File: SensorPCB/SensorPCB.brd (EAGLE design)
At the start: 36 x 66 mm, 31 parts, among them T1 33u

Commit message: 3v almost ready
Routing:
- net +3V3: track 22.2 -> 173.0 mm, vias 1 -> 7
- net I2C1_SDA_SENSOR: track 48.6 -> 71.7 mm, vias 0 -> 2
- net SW_WLAN: track 31.7 -> 32.9 mm
- net PB0: track 69.9 -> 69.0 mm
- net USART2_RX_SENSOR: track 122.6 -> 123.3 mm
- net SWCLK: track 10.4 -> 9.71 mm

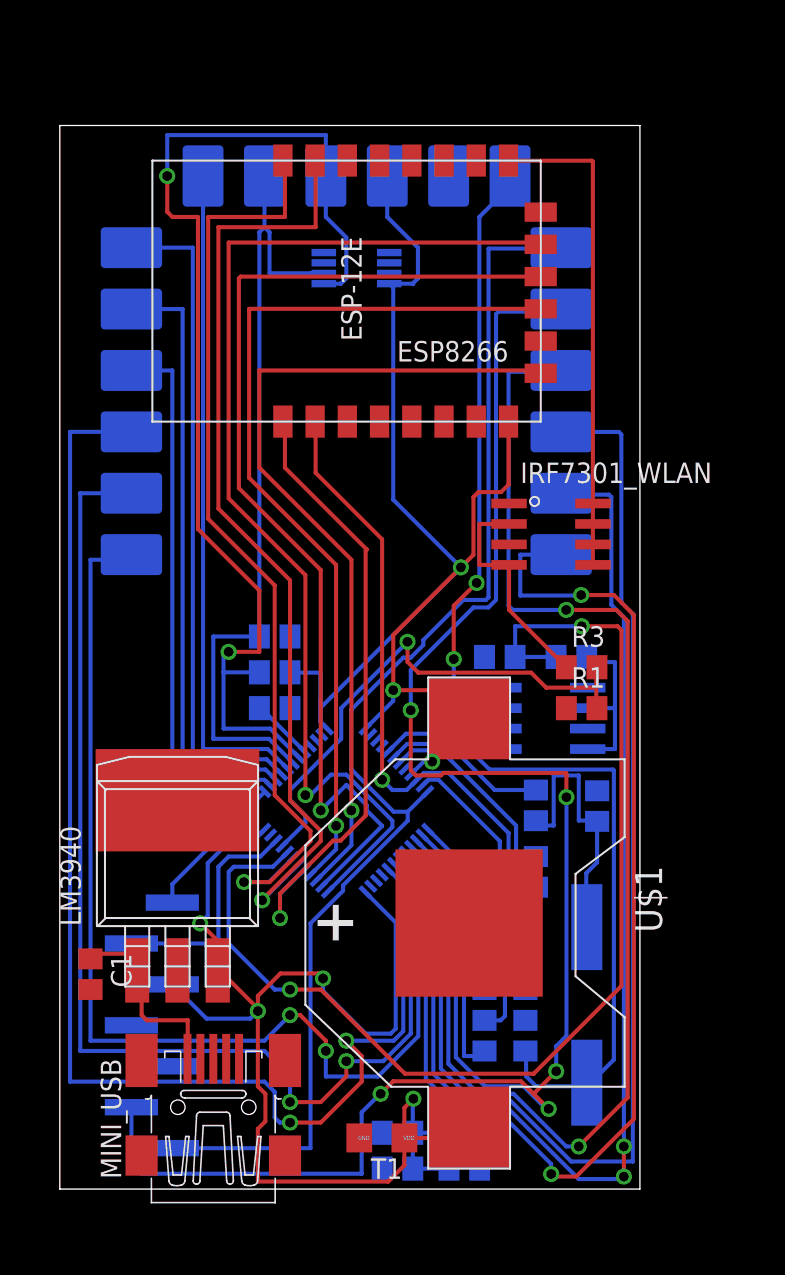
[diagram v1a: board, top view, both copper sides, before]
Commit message: routed all 3v wires
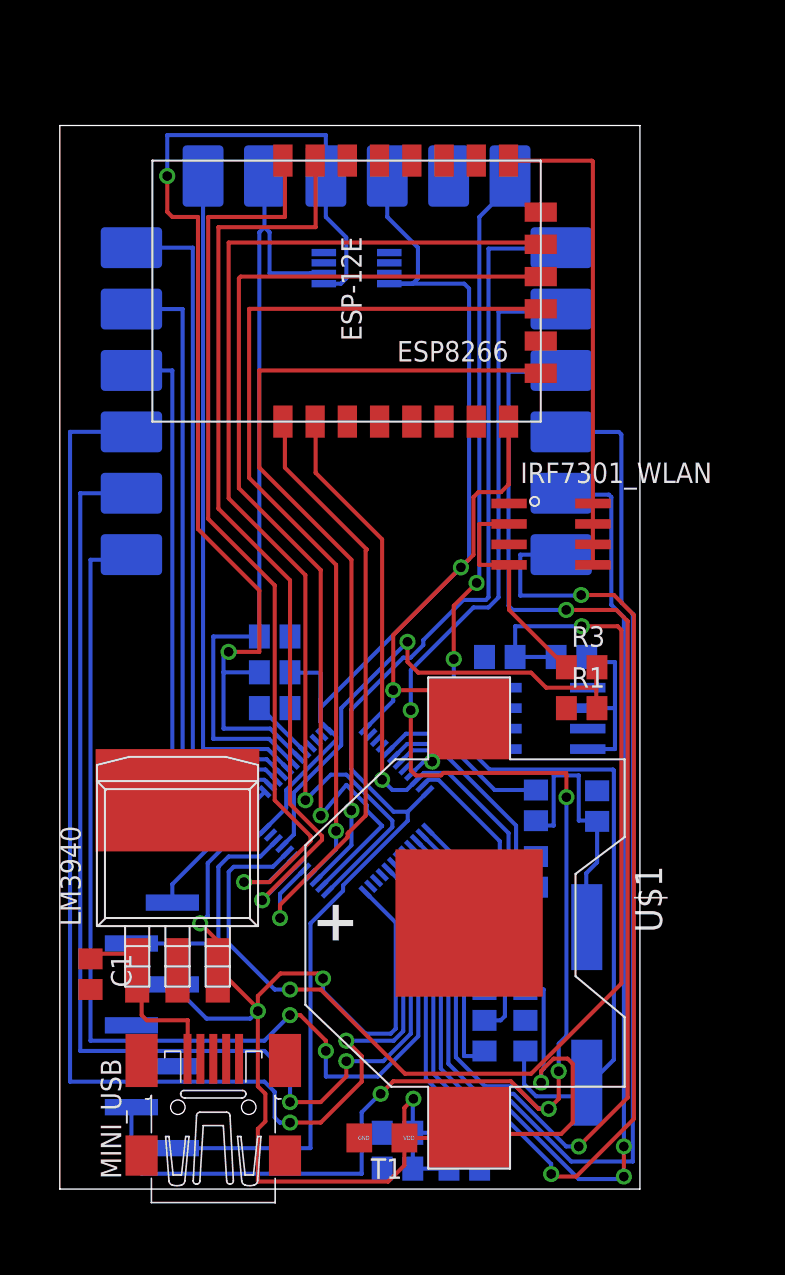
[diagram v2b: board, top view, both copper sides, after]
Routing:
- net +3V3: track 173.0 -> 204.4 mm, vias 7 -> 8
- net OSC_IN: track 41.6 -> 42.8 mm
- net SW_WLAN: track 32.9 -> 32.1 mm
- net SPI2_SCK_WLAN: track 64.9 -> 65.5 mm
- net USART2_RX_SENSOR: track 123.3 -> 123.8 mm

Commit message: start new board version
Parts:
- removed MINI_USB: MINI-USB-SCHIELD-32005-201, con-cypressindustries:32005-201
- added R4: 10k, rcl:R0805
- added U$2: 5V_POWER_SUPPLY, 5V_POWER_SUPPLY:5V_POWER_SUPPLY
- moved T1 30.8 mm to (6.99, 31.1)
- moved R1 27.8 mm to (5.08, 24.8), flipped to the bottom, turned to 180 degrees
- moved R6 24.7 mm to (5.08, 22.2)
- moved C6 21.3 mm to (34.6, 2.54), flipped to the top, turned to 0 degrees
- moved R10 20.9 mm to (34.0, 28.9)
- moved R3 20.6 mm to (12.1, 35.6)
- moved ESP8266 19.1 mm to (10.8, 45.7), turned to 0 degrees
- moved R11 19.1 mm to (34.6, 5.40), flipped to the top, turned to 0 degrees
- moved IRF7301_WLAN 18.5 mm to (12.1, 39.4)
- moved R7 18.2 mm to (34.0, 26.0), turned to 0 degrees
- moved C1 17.8 mm to (2.22, 31.1), turned to 180 degrees
- moved QUARZ-HC49 14.1 mm to (34.3, 25.4), flipped to the top, turned to 90 degrees
- moved C8 12.9 mm to (15.2, 9.53), turned to 0 degrees
- moved C10 12.9 mm to (34.0, 31.8), turned to 0 degrees
- moved C3 12.8 mm to (15.2, 12.7)
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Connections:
- removed net CH_PD_WLAN: ESP8266.3
- removed net D+: MINI_USB.3
- removed net D-: MINI_USB.2
- removed net ID: MINI_USB.4
- new net ADC: R7.2, R8.1, STM32L051C8T6.10
- new net CHPD: ESP8266.3, R4.1
- net +3V3: now also R4.2
- net +5V: now also U$2.MINUS; no longer MINI_USB.1
- net ADC_WLAN: no longer R7.2, R8.1, STM32L051C8T6.10
- net GND: now also U$2.PLUS; no longer MINI_USB.5
- net SPI2_MISO_WLAN: no longer STM32L051C8T6.27
- net SPI2_MOSI_WLAN: no longer STM32L051C8T6.28
- net SPI2_NSS_WLAN: no longer STM32L051C8T6.25
- net SPI2_SCK_WLAN: no longer STM32L051C8T6.26
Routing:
- net +3V3: track 204.4 -> 0.00 mm, vias 8 -> 0
- net USART2_RX_SENSOR: track 123.8 -> 0.00 mm, vias 5 -> 0
- net PA4: track 84.7 -> 0.00 mm, vias 2 -> 0
- net PB2: track 82.4 -> 0.00 mm, vias 2 -> 0
- net USART2_TX_SENSOR: track 80.1 -> 0.00 mm
- net PA5: track 78.3 -> 0.00 mm
- net PA7: track 75.8 -> 0.00 mm, vias 2 -> 0
- net PA6: track 75.1 -> 0.00 mm, vias 2 -> 0
- net PB1: track 73.9 -> 0.00 mm, vias 2 -> 0
- net SW_SENSOR: track 71.7 -> 0.00 mm, vias 2 -> 0
- net I2C1_SDA_SENSOR: track 71.7 -> 0.00 mm, vias 2 -> 0
- net SPI2_NSS_WLAN: track 69.3 -> 0.00 mm, vias 1 -> 0
- net PB0: track 69.0 -> 0.00 mm, vias 2 -> 0
- net SPI2_SCK_WLAN: track 65.5 -> 0.00 mm, vias 1 -> 0
- net USART1_TX_WLAN: track 59.4 -> 0.00 mm, vias 1 -> 0
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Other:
- board size 36 x 66 mm -> 37 x 70 mm

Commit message: some changes
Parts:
- moved R10 31.5 mm to (2.54, 26.4)
- moved PHD 20.7 mm to (24.4, 3.81), turned to 0 degrees
- moved C3 19.8 mm to (34.9, 10.5), turned to 270 degrees
- moved R6 10.2 mm to (7.94, 12.4)
- moved R1 9.94 mm to (7.94, 15.2)
- moved C5 8.90 mm to (30.5, 12.4), turned to 0 degrees
- moved C7 8.89 mm to (30.5, 9.53), turned to 0 degrees
- moved C8 7.30 mm to (7.94, 9.53), turned to 180 degrees
- moved C9 6.43 mm to (30.5, 15.2), turned to 180 degrees
- moved R9 5.97 mm to (2.54, 23.8)
- moved R8 3.19 mm to (34.3, 26.4), turned to 180 degrees
- moved R12 3.17 mm to (2.54, 28.9)
- moved C10 2.88 mm to (34.3, 28.9), turned to 180 degrees
- moved R7 2.25 mm to (34.3, 23.8)
- moved MCP9808 1.93 mm to (19.1, 55.6)
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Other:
- board size 37 x 70 mm -> 37 x 65 mm

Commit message: routing
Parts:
- moved C1 24.9 mm to (3.17, 6.19), turned to 0 degrees
- moved C4 23.5 mm to (34.1, 37.8), turned to 270 degrees
- moved U$2 23.3 mm to (5.40, 2.38), turned to 180 degrees
- moved MCP9808 20.3 mm to (3.97, 69.2)
- moved C6 15.3 mm to (35.6, 17.8), turned to 90 degrees
- moved IRF7301_SENSOR 12.7 mm to (12.1, 39.4)
- moved IRF7301_WLAN 12.7 mm to (24.8, 39.4)
- moved R2 12.7 mm to (12.1, 35.6)
- moved R3 12.7 mm to (24.8, 35.6)
- moved R11 12.5 mm to (32.7, 17.8), turned to 90 degrees
- moved LM3940 11.2 mm to (6.67, 24.1), turned to 0 degrees
- moved STM32L051C8T6 3.82 mm to (18.5, 23.0)
- moved T1 2.66 mm to (9.53, 31.9)
- moved U$1 2.54 mm to (21.0, 9.68)
- moved QUARZ-HC49 2.23 mm to (34.1, 27.6)
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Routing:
- net USART2_RX_SENSOR: track 0.00 -> 62.0 mm, vias 0 -> 2
- net USART2_TX_SENSOR: track 0.00 -> 60.0 mm, vias 0 -> 2
- net I2C1_SDA_SENSOR: track 0.00 -> 43.3 mm
- net PB2: track 0.00 -> 42.0 mm
- net I2C1_SCL_SENSOR: track 0.00 -> 40.5 mm
- net SPI1_MOSI_SENSOR: track 0.00 -> 37.9 mm
- net SPI1_MISO_SENSOR: track 0.00 -> 37.7 mm
- net PB1: track 0.00 -> 37.1 mm
- net PA4: track 0.00 -> 37.0 mm
- net PA5: track 0.00 -> 34.1 mm
- net SPI1_SCK_SENSOR: track 0.00 -> 33.6 mm
- net PB0: track 0.00 -> 32.2 mm
- net PA6: track 0.00 -> 31.1 mm
- net SPI1_NSS_SENSOR: track 0.00 -> 29.6 mm
- net OSC_OUT: track 0.00 -> 28.5 mm, vias 0 -> 3
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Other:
- board text added: "+5V"
- board text added: "GND"

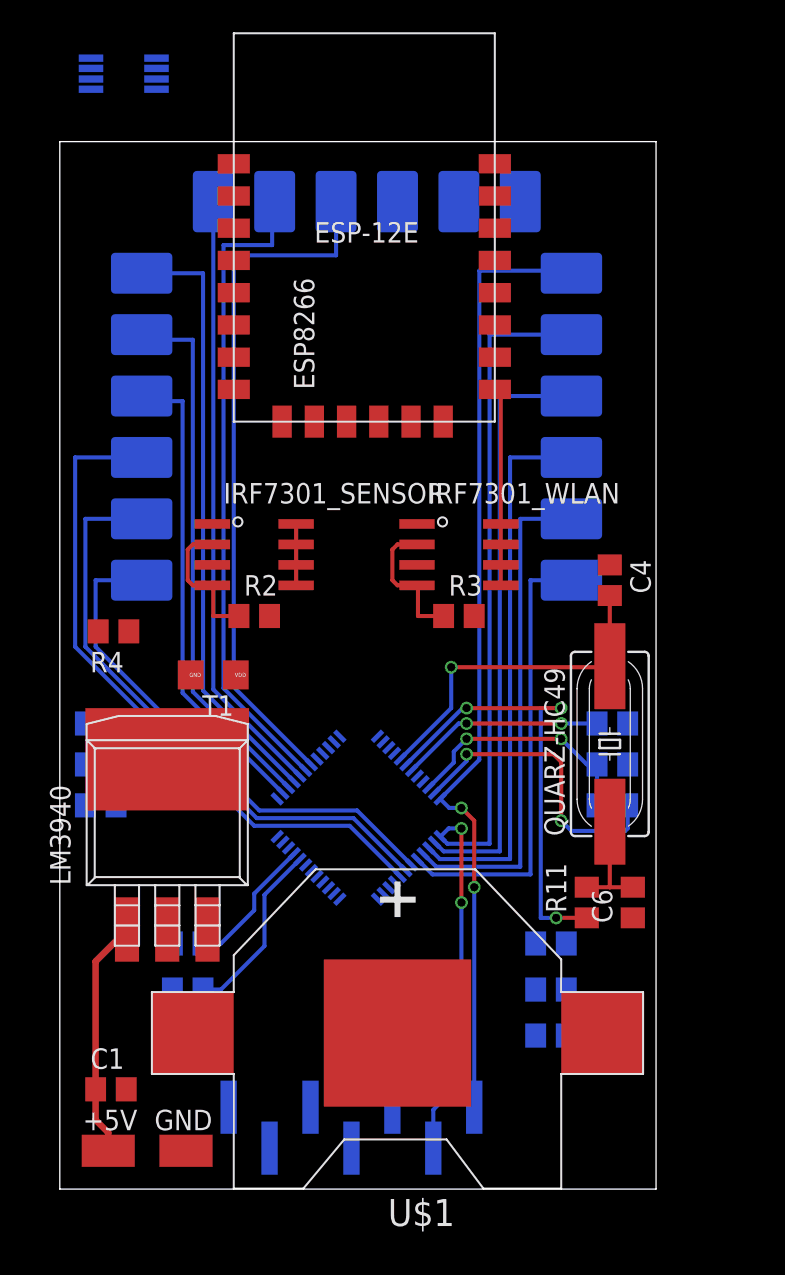
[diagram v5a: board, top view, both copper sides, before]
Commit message: delet temp sensor + route all signal wires
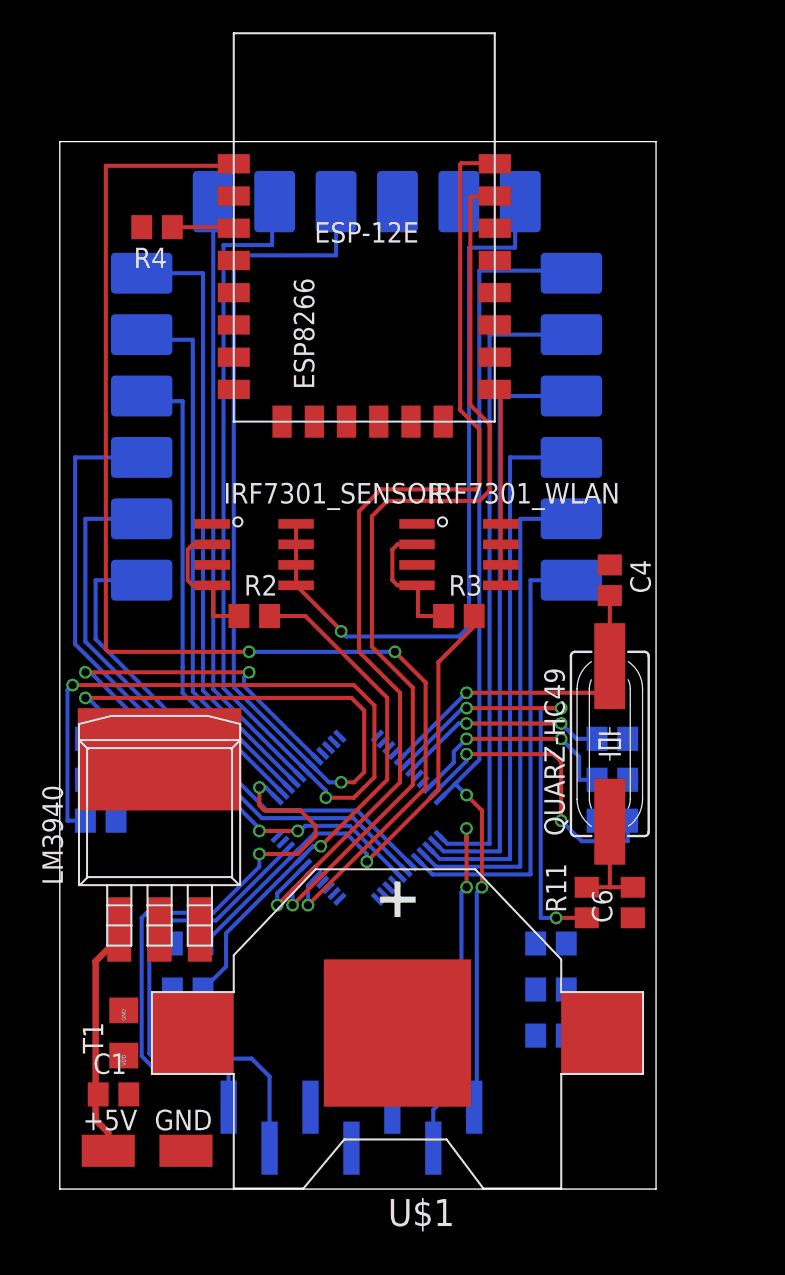
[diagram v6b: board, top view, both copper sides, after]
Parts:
- removed MCP9808: MCP9808-E/MS, mcp9808:SOP65P490X110-8N
- moved R4 25.2 mm to (6.03, 59.7)
- moved T1 22.9 mm to (3.97, 9.68), turned to 90 degrees
- moved R12 3.49 mm to (2.54, 25.4)
- moved R10 1.59 mm to (2.54, 27.9)
- moved R7 0.95 mm to (34.3, 22.9)
- moved R8 0.95 mm to (34.3, 25.4)
- moved R9 0.95 mm to (2.54, 22.9), turned to 180 degrees
- moved C10 0.95 mm to (34.3, 27.9)
- moved LM3940 0.48 mm to (6.19, 24.1)
- moved C1 0.35 mm to (3.33, 5.87)
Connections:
- removed net ALERT: MCP9808.3
- net +3V3: no longer MCP9808.8
- net GND: no longer MCP9808.4, MCP9808.5, MCP9808.6, MCP9808.7
- net I2C1_SCL_SENSOR: no longer MCP9808.2
- net I2C1_SDA_SENSOR: no longer MCP9808.1
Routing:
- net REST_WLAN: track 0.00 -> 77.5 mm, vias 0 -> 3
- net USART1_RX_WLAN: track 0.00 -> 62.6 mm, vias 0 -> 1
- net USART1_TX_WLAN: track 0.00 -> 59.1 mm, vias 0 -> 1
- net GND_SENSOR: track 3.81 -> 45.5 mm, vias 0 -> 1
- net I2C1_SCL_SENSOR: track 40.5 -> 79.6 mm, vias 0 -> 2
- net SWCLK: track 0.00 -> 37.2 mm, vias 0 -> 2
- net SWDIO: track 0.00 -> 31.2 mm
- net N$8: track 0.00 -> 30.8 mm, vias 0 -> 2
- net I2C1_SDA_SENSOR: track 43.3 -> 72.1 mm, vias 0 -> 2
- net SW_WLAN: track 8.58 -> 32.0 mm, vias 0 -> 1
- net SW_SENSOR: track 11.2 -> 32.5 mm, vias 0 -> 1
- net CHPD: track 0.00 -> 3.84 mm
- net +5V: track 15.7 -> 16.7 mm
- net ADC: track 15.7 -> 16.5 mm
- net PB2: track 42.0 -> 42.2 mm, vias 0 -> 2

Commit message: routed +3v
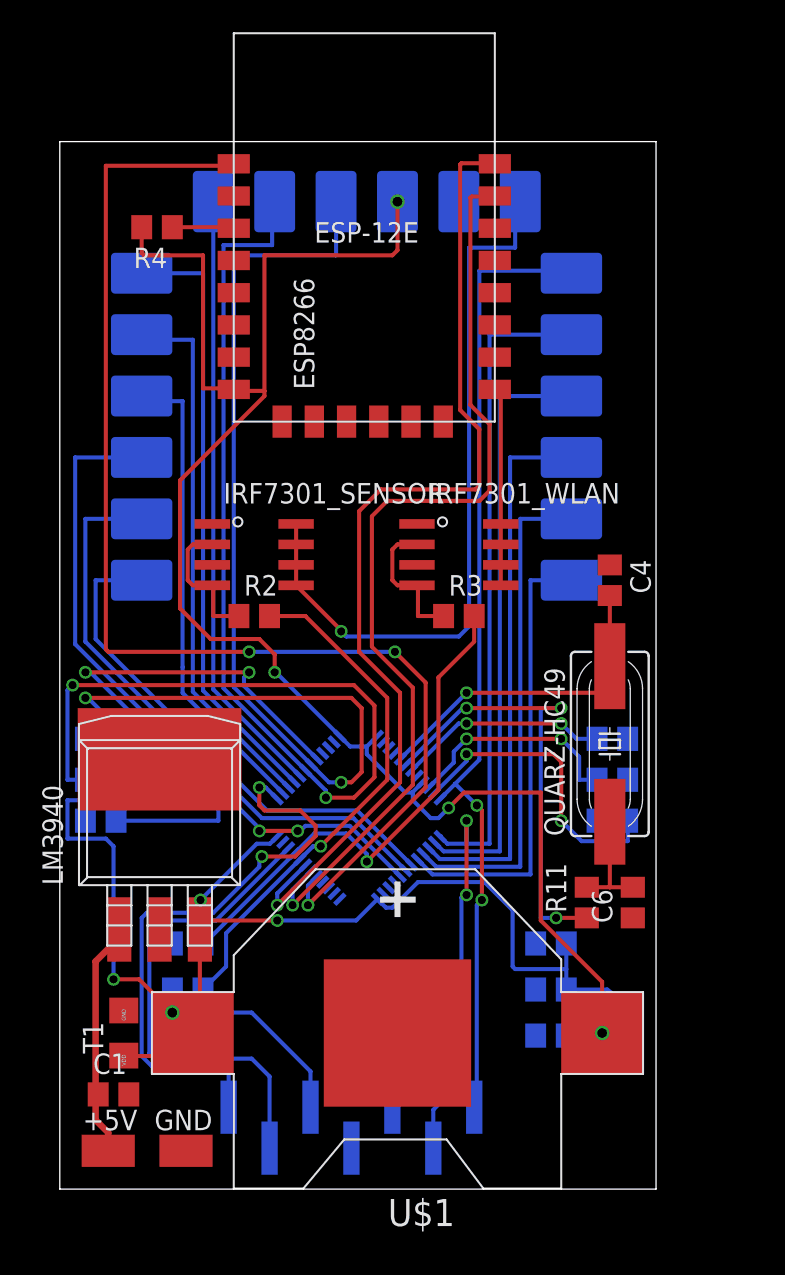
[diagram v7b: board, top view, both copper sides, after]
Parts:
- moved R12 2.54 mm to (2.54, 22.9)
- moved R9 2.54 mm to (2.54, 25.4)
- moved C3 0.32 mm to (35.2, 10.5)
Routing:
- net +3V3: track 0.00 -> 208.5 mm, vias 0 -> 8
- net N$8: track 30.8 -> 36.7 mm
- net I2C1_SCL_SENSOR: track 79.6 -> 77.1 mm
- net USART2_RX_SENSOR: track 61.7 -> 62.7 mm

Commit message: some changes
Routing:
- net GND: track 0.00 -> 25.0 mm, vias 0 -> 3
- net SWCLK: track 37.0 -> 31.8 mm
- net +3V3: track 208.5 -> 209.0 mm
- added copper zone on layer 1, net GND
- added copper zone on layer 16, net GND
